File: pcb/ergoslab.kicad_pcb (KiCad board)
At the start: 2 copper layers, 114.5 x 101.2 mm, 102 parts, among them J1 L_B_LED, J2 R_B_LED, J3 SLAVE_LED, P1 OLED, P2 ICSP, SW0:0 SW_Push, SW0:1 SW_Push, SW0:2 SW_Push, SW0:3 SW_Push, SW0:4 SW_Push, SW1:0 SW_Push, SW1:1 SW_Push, SW1:2 SW_Push, SW1:3 SW_Push, SW1:4 SW_Push, SW2:0 SW_Push, SW2:1 SW_Push, SW2:2 SW_Push, SW2:3 SW_Push, SW2:4 SW_Push, SW3:0 SW_Push, SW3:1 SW_Push, SW3:2 SW_Push, SW3:3 SW_Push, SW3:4 SW_Push, SW3:5 SW_Push, SW4:1 SW_Push, SW4:2 SW_Push, SW4:3 SW_Push, SW4:4 SW_Push, SW4:5 SW_Push

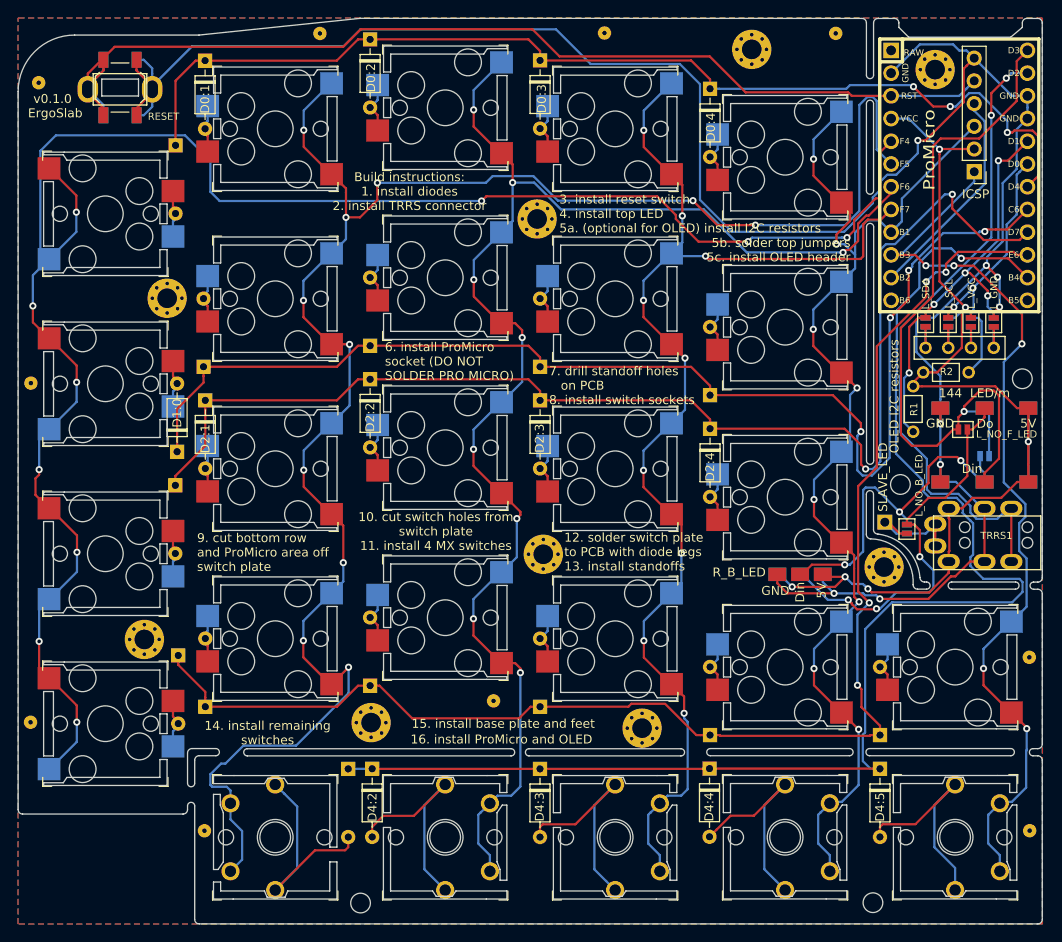
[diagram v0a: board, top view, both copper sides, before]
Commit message: fix: increase all snap-off supports to at least 3mm as per JLCPCB requirements
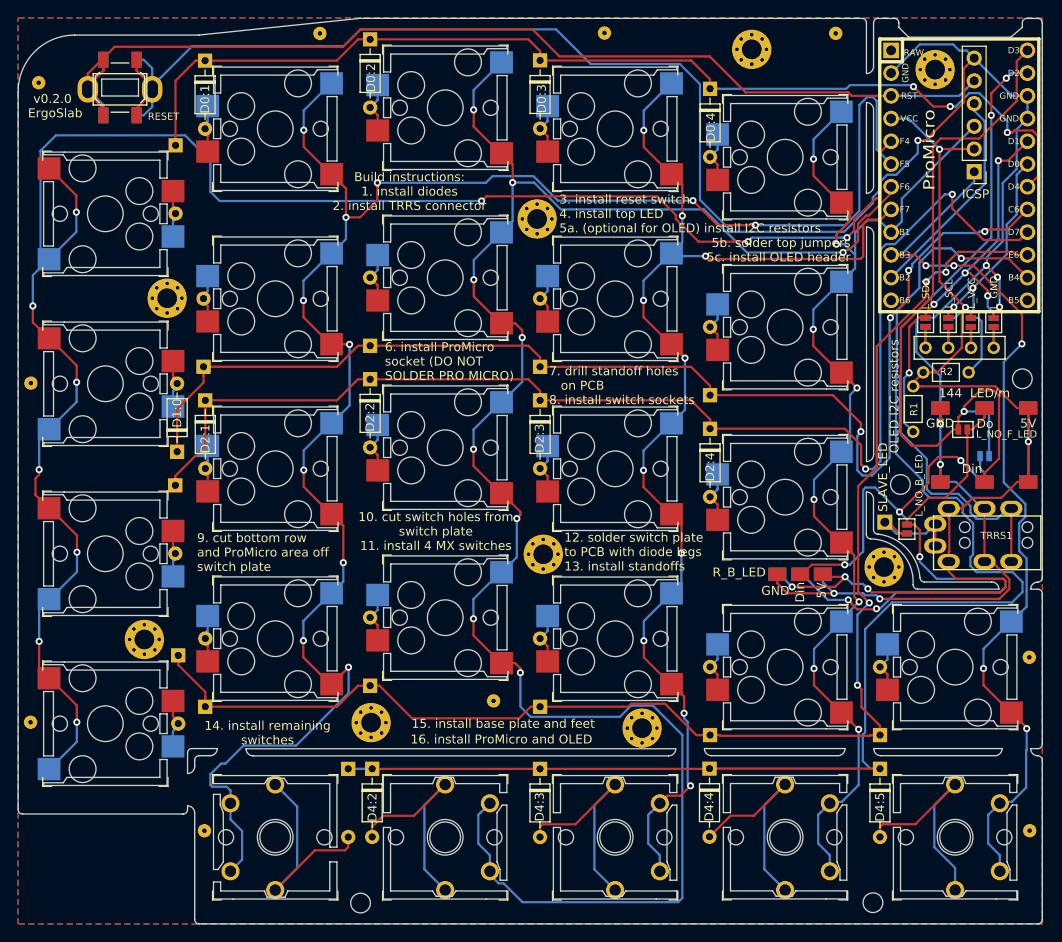
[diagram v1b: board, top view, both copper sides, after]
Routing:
- net Col2: track 162.6 -> 211.5 mm
- net Net-(J1-Pad2): track 44.4 -> 60.1 mm
- net VCC: track 117.8 -> 130.8 mm
- net GND: track 261.3 -> 267.5 mm
- net Col3: track 134.8 -> 135.1 mm, vias 9 -> 10
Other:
- outline, holes or cut-outs redrawn
- board text added: "v0.2.0"
- board text removed: "v0.1.0"

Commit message: fix: test making switch plate cutout the correct size on SW4:4
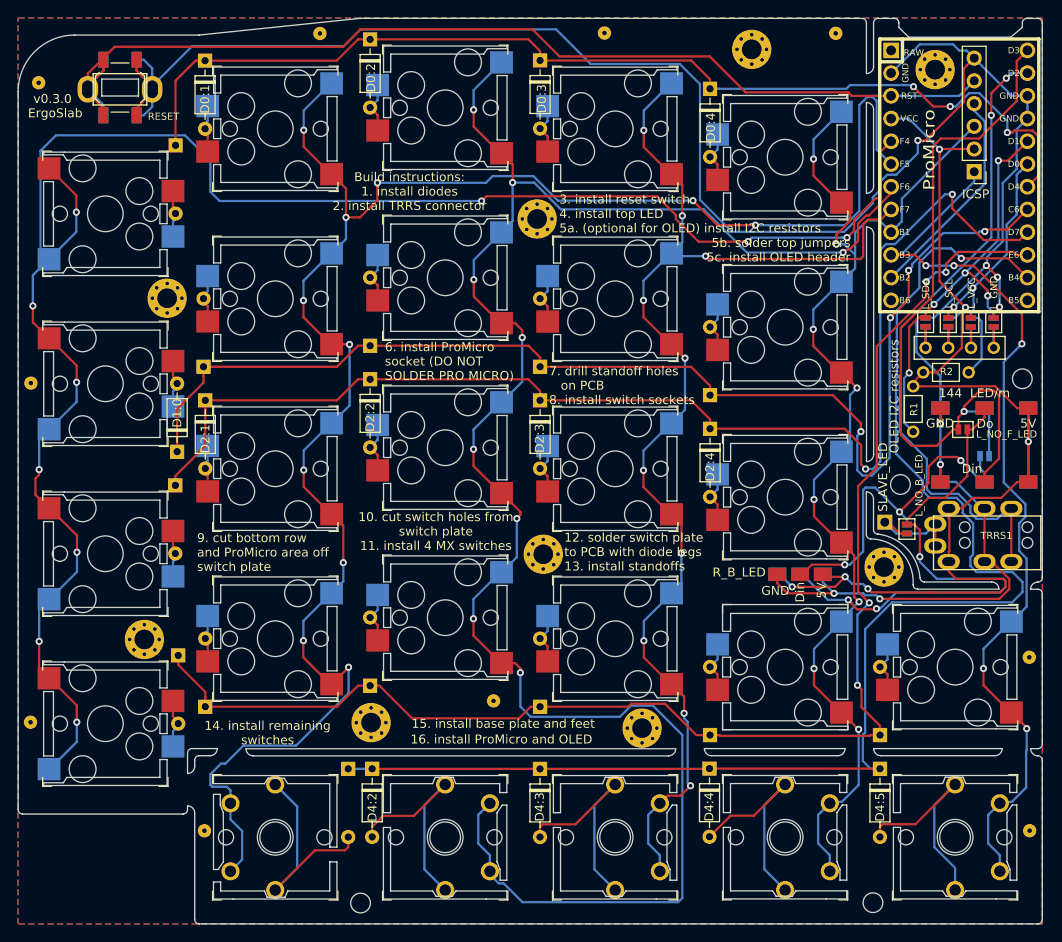
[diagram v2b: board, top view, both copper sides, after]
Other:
- outline, holes or cut-outs redrawn
- board text added: "v0.3.0"
- board text removed: "v0.2.0"
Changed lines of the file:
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@@
-(kicad_pcb (version 20171130) (host pcbnew 5.1.4)
+(kicad_pcb (version 20171130) (host pcbnew 5.1.5)
   (general
     (thickness 1.6)
-    (drawings 782)
+    (drawings 781)
     (tracks 1180)
     (zones 0)
@@
   (title_block
     (title ErgoSlab)
-    (rev 0.2.0)
+    (rev 0.3.0)
     (company "By Tom Saleeba")
     (comment 1 "MIT License")
@@
     (41 Cmts.User user)
     (42 Eco1.User user)
-    (43 Eco2.User user)
+    (43 Eco2.User user hide)
     (44 Edge.Cuts user)
     (45 Margin user)
@@
   (gr_line (start 133.1 112.455) (end 133.1 114.655) (layer Edge.Cuts) (width 0.05))
   (gr_line (start 133.1 114.655) (end 132.3 114.655) (layer Edge.Cuts) (width 0.05))
-  (gr_line (start 151.3 115.625) (end 152.1 115.625) (layer Edge.Cuts) (width 0.05))
-  (gr_line (start 162.9 110.125) (end 165.1 110.125) (layer Edge.Cuts) (width 0.05))
-  (gr_line (start 165.1 109.825) (end 151.3 109.825) (layer Edge.Cuts) (width 0.05))
+  (gr_line (start 151.2 115.625) (end 152.1 115.625) (layer Edge.Cuts) (width 0.05))
+  (gr_line (start 162.9 110.125) (end 165.2 110.125) (layer Edge.Cuts) (width 0.05))
+  (gr_line (start 165.2 109.73) (end 151.2 109.73) (layer Edge.Cuts) (width 0.05))
   (gr_line (start 162.9 110.125) (end 162.5 110.725) (layer Edge.Cuts) (width 0.05))
-  (gr_line (start 165.1 120.325) (end 164 120.325) (layer Edge.Cuts) (width 0.05))
-  (gr_line (start 162.8 123.625) (end 165.1 123.625) (layer Edge.Cuts) (width 0.05))
-  (gr_line (start 151.3 112.725) (end 151.3 109.825) (layer Edge.Cuts) (width 0.05))
+  (gr_line (start 165.2 120.325) (end 164 120.325) (layer Edge.Cuts) (width 0.05))
+  (gr_line (start 151.2 112.725) (end 151.2 109.73) (layer Edge.Cuts) (width 0.05))
   (gr_line (start 162.9 123.325) (end 162.5 122.725) (layer Edge.Cuts) (width 0.05))
-  (gr_line (start 151.3 120.725) (end 151.3 123.625) (layer Edge.Cuts) (width 0.05))
-  (gr_line (start 164 113.125) (end 165.1 113.125) (layer Edge.Cuts) (width 0.05))
+  (gr_line (start 151.2 120.725) (end 151.2 123.72) (layer Edge.Cuts) (width 0.05))
+  (gr_line (start 164 113.125) (end 165.2 113.125) (layer Edge.Cuts) (width 0.05))
   (gr_line (start 152.1 110.725) (end 152.1 112.725) (layer Edge.Cuts) (width 0.05))
   (gr_line (start 152.1 122.725) (end 162.5 122.725) (layer Edge.Cuts) (width 0.05))
-  (gr_line (start 165.1 113.125) (end 165.1 120.325) (layer Edge.Cuts) (width 0.05))
-  (gr_line (start 151.3 112.725) (end 152.1 112.725) (layer Edge.Cuts) (width 0.05))
-  (gr_line (start 151.3 120.725) (end 152.1 120.725) (layer Edge.Cuts) (width 0.05))
-  (gr_line (start 165.1 123.625) (end 165.1 123.325) (layer Edge.Cuts) (width 0.05))
+  (gr_line (start 165.2 113.125) (end 165.2 120.325) (layer Edge.Cuts) (width 0.05))
+  (gr_line (start 151.2 112.725) (end 152.1 112.725) (layer Edge.Cuts) (width 0.05))
+  (gr_line (start 151.2 120.725) (end 152.1 120.725) (layer Edge.Cuts) (width 0.05))
+  (gr_line (start 165.2 123.72) (end 165.2 123.325) (layer Edge.Cuts) (width 0.05))
   (gr_line (start 152.1 115.625) (end 152.1 117.825) (layer Edge.Cuts) (width 0.05))
   (gr_line (start 164 120.325) (end 164 113.125) (layer Edge.Cuts) (width 0.05))
-  (gr_line (start 162.8 123.625) (end 151.3 123.625) (layer Edge.Cuts) (width 0.05))
+  (gr_line (start 165.2 123.72) (end 151.2 123.72) (layer Edge.Cuts) (width 0.05))
   (gr_line (start 162.5 110.725) (end 152.1 110.725) (layer Edge.Cuts) (width 0.05))
-  (gr_line (start 165.1 123.325) (end 162.9 123.325) (layer Edge.Cuts) (width 0.05))
+  (gr_line (start 165.2 123.325) (end 162.9 123.325) (layer Edge.Cuts) (width 0.05))
   (gr_line (start 152.1 122.725) (end 152.1 120.725) (layer Edge.Cuts) (width 0.05))
-  (gr_line (start 152.1 117.825) (end 151.3 117.825) (layer Edge.Cuts) (width 0.05))
-  (gr_line (start 151.3 117.825) (end 151.3 115.625) (layer Edge.Cuts) (width 0.05))
-  (gr_line (start 165.1 109.825) (end 165.1 110.125) (layer Edge.Cuts) (width 0.05))
+  (gr_line (start 152.1 117.825) (end 151.2 117.825) (layer Edge.Cuts) (width 0.05))
+  (gr_line (start 151.2 117.825) (end 151.2 115.625) (layer Edge.Cuts) (width 0.05))
+  (gr_line (start 165.2 109.73) (end 165.2 110.125) (layer Edge.Cuts) (width 0.05))
   (gr_line (start 92.19 127.82) (end 92.19 127.13) (layer Edge.Cuts) (width 0.05))
   (gr_line (start 91.39 128.62) (end 91.39 126.33) (layer Edge.Cuts) (width 0.05))
@@
   (gr_line (start 167.28 53.61) (end 167.28 63.76) (layer Edge.Cuts) (width 0.05))
   (gr_line (start 168.08 54.41) (end 168.08 62.96) (layer Edge.Cuts) (width 0.05))
-  (gr_text v0.2.0 (at 76.3 53.2) (layer F.SilkS)
+  (gr_text v0.3.0 (at 76.3 53.2) (layer F.SilkS)
     (effects (font (size 1 1) (thickness 0.15)))
   )
